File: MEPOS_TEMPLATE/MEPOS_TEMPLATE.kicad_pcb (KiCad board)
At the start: 4 copper layers, 101.6 x 101.6 mm, 9 parts, among them J201 Conn_02x32_Odd_Even, J202 Conn_02x20_Odd_Even

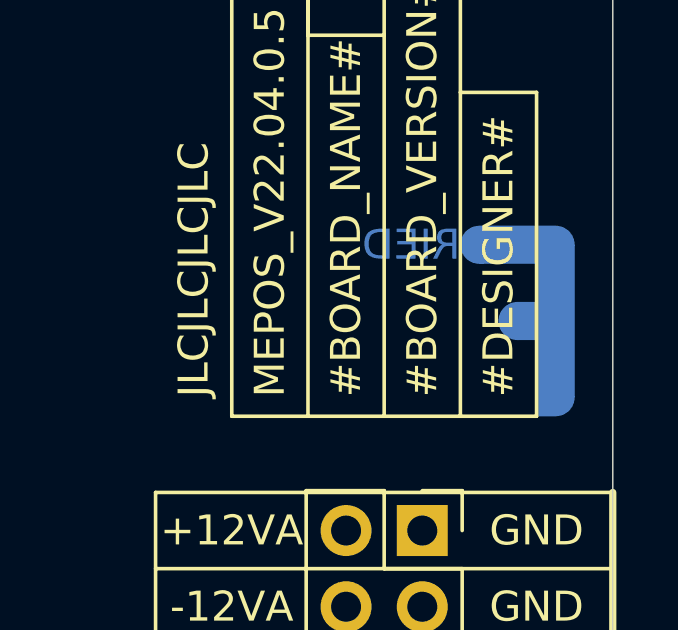
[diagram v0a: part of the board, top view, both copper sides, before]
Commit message: Changed logo to a footprint so that it can be used on other projects
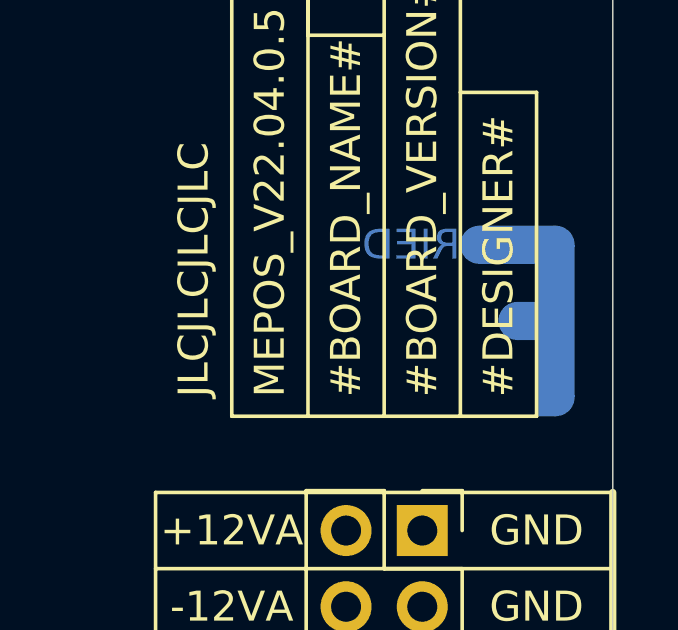
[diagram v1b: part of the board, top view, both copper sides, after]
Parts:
- added REF**: Logo, MEP_TEMPLATE:Logo, F.Cu at (188.1, 68.9)
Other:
- board text removed: "LECTRONICS"
- board text removed: "RIED"
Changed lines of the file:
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@@
     )
+  )
+  (footprint "MEP_TEMPLATE:Logo" (layer "F.Cu")
+    (at 188.09775 68.885)
+    (attr smd)
+    (fp_text reference "REF**" (at 0 -4.445 unlocked) (layer "F.Fab")
+      (effects (font (size 1 1) (thickness 0.15)))
+    )
+    (fp_text value "Logo" (at 0 6.35 unlocked) (layer "F.Fab")
+      (effects (font (size 1 1) (thickness 0.15)))
+    )
+    (fp_text user "RIED" (at 2.54 -2.54) (layer "B.Cu")
+      (effects (font (size 1 1) (thickness 0.15)) (justify left mirror))
+    )
+    (fp_text user "LECTRONICS" (at 2.54 2.54) (layer "B.SilkS")
+      (effects (font (size 1 1) (thickness 0.15)) (justify left mirror))
+    )
+    (fp_text user "RIED" (at 2.54 -2.54) (layer "B.Mask")
+      (effects (font (size 1 1) (thickness 0.15)) (justify left mirror))
+    )
+    (fp_text user "${REFERENCE}" (at 0 4.445 unlocked) (layer "F.Fab")
+      (effects (font (size 1 1) (thickness 0.15)))
+    )
+    (fp_circle (center 3.175 -2.54) (end 3.81 -2.54) (layer "B.Cu") (width 0.001) (fill solid))
+    (fp_circle (center 5.715 -2.54) (end 6.35 -2.54) (layer "B.Cu") (width 0.001) (fill solid))
+    (fp_circle (center 4.445 0) (end 5.08 0) (layer "B.Cu") (width 0.001) (fill solid))
+    (fp_circle (center 5.715 2.54) (end 6.35 2.54) (layer "B.Cu") (width 0.001) (fill solid))
+    (fp_poly (pts
+        (xy 6.35 -2.54)
+        (xy 6.35 2.54)
+        (xy 5.715 3.175)
+        (xy 5.08 3.175)
+        (xy 5.08 0.635)
+        (xy 4.445 0.635)
+        (xy 4.445 -0.635)
+        (xy 5.08 -0.635)
+        (xy 5.08 -1.905)
+        (xy 3.175 -1.905)
+        (xy 3.175 -3.175)
+        (xy 5.715 -3.175)
+      ) (layer "B.Cu") (width 0.001) (fill solid))
+    (fp_circle (center 3.175 2.54) (end 3.81 2.54) (layer "B.SilkS") (width 0.001) (fill solid))
+    (fp_poly (pts
+        (xy 5.08 3.175)
+        (xy 3.175 3.175)
+        (xy 3.175 1.905)
+        (xy 5.08 1.905)
+      ) (layer "B.SilkS") (width 0.001) (fill solid))
+    (fp_circle (center 4.445 0) (end 5.08 0) (layer "B.Mask") (width 0.001) (fill solid))
+    (fp_circle (center 5.715 -2.54) (end 6.35 -2.54) (layer "B.Mask") (width 0.001) (fill solid))
+    (fp_circle (center 5.715 2.54) (end 6.35 2.54) (layer "B.Mask") (width 0.001) (fill solid))
+    (fp_circle (center 3.175 -2.54) (end 3.81 -2.54) (layer "B.Mask") (width 0.001) (fill solid))
+    (fp_poly (pts
+        (xy 6.35 -2.54)
+        (xy 6.35 2.54)
+        (xy 5.715 3.175)
+        (xy 5.08 3.175)
+        (xy 5.08 0.635)
+        (xy 4.445 0.635)
+        (xy 4.445 -0.635)
+        (xy 5.08 -0.635)
+        (xy 5.08 -1.905)
+        (xy 3.175 -1.905)
+        (xy 3.175 -3.175)
+        (xy 5.715 -3.175)
+      ) (layer "B.Mask") (width 0.001) (fill solid))
   )
   (footprint "Symbol:KiCad-Logo2_5mm_SilkScreen" locked (layer "B.Cu")
@@
       ) (layer "B.SilkS") (width 0.01) (fill solid))
   )
-  (gr_poly locked
-    (pts
-      (xy 194.45 66.345)
-      (xy 194.45 71.425)
-      (xy 193.815 72.06)
-      (xy 193.18 72.06)
-      (xy 193.18 69.52)
-      (xy 192.545 69.52)
-      (xy 192.545 68.25)
-      (xy 193.18 68.25)
-      (xy 193.18 66.98)
-      (xy 191.275 66.98)
-      (xy 191.275 65.71)
-      (xy 193.815 65.71)
-    ) (layer "B.Cu") (width 0.001) (fill solid))
-  (gr_circle locked (center 193.815 71.425) (end 194.45 71.425) (layer "B.Cu") (width 0.001) (fill solid))
-  (gr_circle locked (center 193.815 66.345) (end 194.45 66.345) (layer "B.Cu") (width 0.001) (fill solid))
-  (gr_circle locked (center 192.545 68.885) (end 193.18 68.885) (layer "B.Cu") (width 0.001) (fill solid))
-  (gr_circle locked (center 191.275 66.345) (end 191.91 66.345) (layer "B.Cu") (width 0.001) (fill solid))
   (gr_circle (center 190.64 130.48) (end 192.24 130.48) (layer "B.Paste") (width 0.001) (fill solid))
   (gr_circle (center 99.2 130.48) (end 100.8 130.48) (layer "B.Paste") (width 0.001) (fill solid))
@@
   (gr_line locked (start 190.64 125.4) (end 190.64 74.6) (layer "B.SilkS") (width 0.12))
   (gr_line locked (start 190.64 74.6) (end 185.56 74.6) (layer "B.SilkS") (width 0.12))
-  (gr_circle locked (center 191.275 71.425) (end 191.91 71.425) (layer "B.SilkS") (width 0.001) (fill solid))
   (gr_line locked (start 185.56 74.6) (end 185.56 125.4) (layer "B.SilkS") (width 0.12))
-  (gr_poly locked
-    (pts
-      (xy 193.18 72.06)
-      (xy 191.275 72.06)
-      (xy 191.275 70.79)
-      (xy 193.18 70.79)
-    ) (layer "B.SilkS") (width 0.001) (fill solid))
   (gr_line locked (start 180.48 125.4) (end 180.48 74.6) (layer "F.SilkS") (width 0.12))
   (gr_line locked (start 94.12 107.62) (end 109.36 107.62) (layer "F.SilkS") (width 0.12))
@@
   (gr_line locked (start 94.12 77.14) (end 109.36 77.14) (layer "F.SilkS") (width 0.12))
   (gr_line locked (start 180.48 94.92) (end 195.72 94.92) (layer "F.SilkS") (width 0.12))
-  (gr_circle locked (center 193.815 66.345) (end 194.45 66.345) (layer "B.Mask") (width 0.001) (fill solid))
-  (gr_circle locked (center 192.545 68.885) (end 193.18 68.885) (layer "B.Mask") (width 0.001) (fill solid))
-  (gr_circle locked (center 191.275 66.345) (end 191.91 66.345) (layer "B.Mask") (width 0.001) (fill solid))
-  (gr_poly locked
-    (pts
-      (xy 194.45 66.345)
-      (xy 194.45 71.425)
-      (xy 193.815 72.06)
-      (xy 193.18 72.06)
-      (xy 193.18 69.52)
-      (xy 192.545 69.52)
-      (xy 192.545 68.25)
-      (xy 193.18 68.25)
-      (xy 193.18 66.98)
-      (xy 191.275 66.98)
-      (xy 191.275 65.71)
-      (xy 193.815 65.71)
-    ) (layer "B.Mask") (width 0.001) (fill solid))
-  (gr_circle locked (center 193.815 71.425) (end 194.45 71.425) (layer "B.Mask") (width 0.001) (fill solid))
   (gr_line locked (start 198.26 105.08) (end 91.58 105.08) (layer "Dwgs.User") (width 0.15))
   (gr_line locked (start 185.56 31.42) (end 185.56 138.1) (layer "Dwgs.User") (width 0.15))
@@
   (gr_arc locked (start 94.12 39.04) (mid 95.607898 35.447898) (end 99.2 33.96) (layer "Edge.Cuts") (width 0.05))
   (gr_line locked (start 190.64 135.56) (end 99.2 135.56) (layer "Edge.Cuts") (width 0.05))
-  (gr_text "RIED" (at 190.64 66.345) (layer "B.Cu")
-    (effects (font (size 1 1) (thickness 0.15)) (justify left mirror))
-  )
   (gr_text "GND" (at 193.18 124.13) (layer "B.SilkS")
     (effects (font (size 1 1) (thickness 0.15)) (justify mirror))
@@
   (gr_text "GND" (at 183.02 83.49) (layer "B.SilkS")
     (effects (font (size 1 1) (thickness 0.15)) (justify mirror))
-  )
-  (gr_text "LECTRONICS" (at 190.64 71.425) (layer "B.SilkS")
-    (effects (font (size 1 1) (thickness 0.15)) (justify left mirror))
   )
   (gr_text "+12V" (at 106.82 50.47) (layer "F.SilkS")
@@
     (effects (font (size 1 1) (thickness 0.15)))
   )
-  (gr_text "RIED" (at 190.64 66.345) (layer "B.Mask")
-    (effects (font (size 1 1) (thickness 0.15)) (justify left mirror))
-  )
   (gr_text "FRONT" (at 144.92 153.34) (layer "Dwgs.User")

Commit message: Updated Libraries
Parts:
- removed the REF** at (188.1, 68.9)
- added REF**: Logo, MEPOS:Logo, F.Cu at (188.1, 68.9)
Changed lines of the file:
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@@
     )
   )
-  (footprint "MEP_TEMPLATE:Logo" (layer "F.Cu")
-    (at 188.09775 68.885)
+  (footprint "MEPOS:Logo" (layer "F.Cu")
+    (at 188.1 68.885)
     (attr smd)
     (fp_text reference "REF**" (at 0 -4.445 unlocked) (layer "F.Fab")
@@
     )
     (fp_circle (center 3.175 -2.54) (end 3.81 -2.54) (layer "B.Cu") (width 0.001) (fill solid))
+    (fp_circle (center 4.445 0) (end 5.08 0) (layer "B.Cu") (width 0.001) (fill solid))
     (fp_circle (center 5.715 -2.54) (end 6.35 -2.54) (layer "B.Cu") (width 0.001) (fill solid))
-    (fp_circle (center 4.445 0) (end 5.08 0) (layer "B.Cu") (width 0.001) (fill solid))
     (fp_circle (center 5.715 2.54) (end 6.35 2.54) (layer "B.Cu") (width 0.001) (fill solid))
     (fp_poly (pts
@@
     (fp_circle (center 4.445 0) (end 5.08 0) (layer "B.Mask") (width 0.001) (fill solid))
     (fp_circle (center 5.715 -2.54) (end 6.35 -2.54) (layer "B.Mask") (width 0.001) (fill solid))
+    (fp_circle (center 3.175 -2.54) (end 3.81 -2.54) (layer "B.Mask") (width 0.001) (fill solid))
     (fp_circle (center 5.715 2.54) (end 6.35 2.54) (layer "B.Mask") (width 0.001) (fill solid))
-    (fp_circle (center 3.175 -2.54) (end 3.81 -2.54) (layer "B.Mask") (width 0.001) (fill solid))
     (fp_poly (pts
         (xy 6.35 -2.54)
